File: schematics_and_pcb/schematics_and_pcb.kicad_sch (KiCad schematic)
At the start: 84 parts, among them J1 RND 205-00623, J2 RND 205-00627, J3 Motor con, J4 Conn_01x04_Male, J5 Conn_01x04_Male, Q1 PMV213SN, SW1 RND 210-00210, U1 MIC5235YM5-TR, U2 AP2125N-3.3TRG1, U3 PWM3389DM-T3QU, U4 STM32F411RETx, Y1 YLFXTAL029370

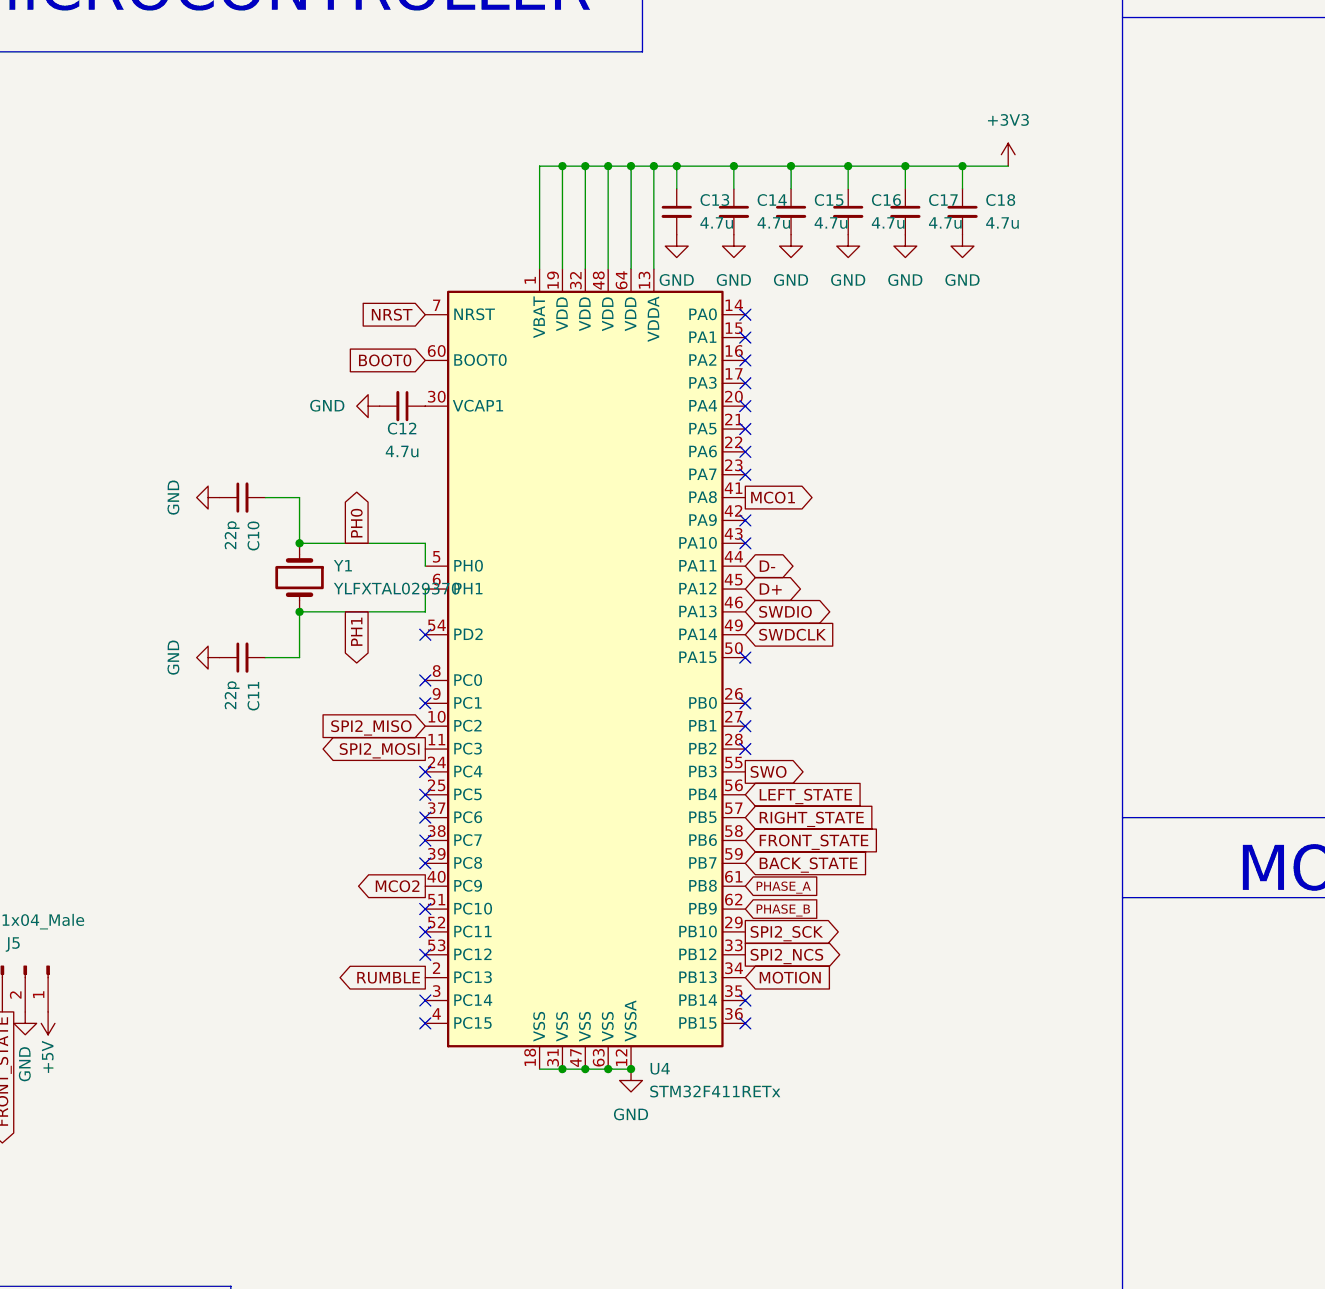
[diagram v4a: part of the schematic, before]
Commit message: added routes for all signals except buttons and scrollwheel
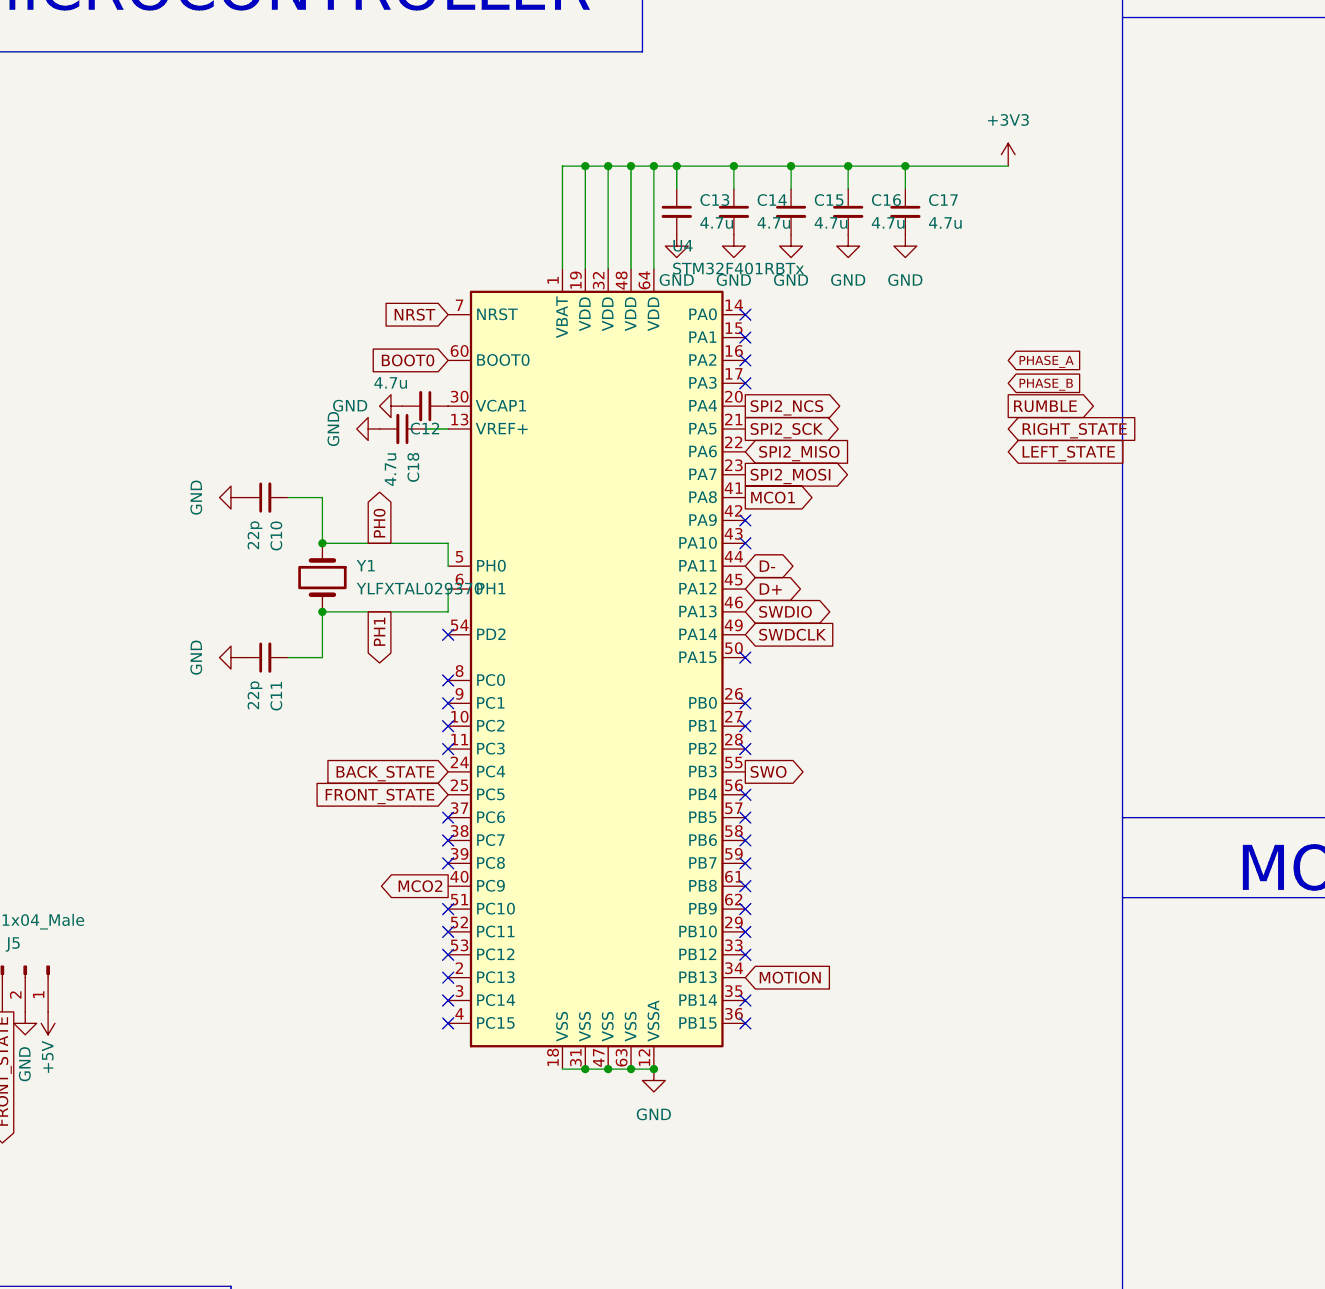
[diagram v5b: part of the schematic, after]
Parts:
- removed U4: STM32F411RETx, Package_QFP:LQFP-64_10x10mm_P0.5mm, symbol MCU_ST_STM32F4:STM32F411RETx
- added U4: STM32F401RBTx, Package_QFP:LQFP-64_10x10mm_P0.5mm, symbol MCU_ST_STM32F4:STM32F401RBTx
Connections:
- net +3V3: now also U4.1 (VBAT), U4.19 (VDD), U4.32 (VDD), U4.48 (VDD), U4.64 (VDD); no longer C18.1
- net BACK_STATE: now also U4.24 (PC4)
- net BOOT0: now also U4.60 (BOOT0)
- net D+: now also U4.45 (PA12)
- net D-: now also U4.44 (PA11)
- net FRONT_STATE: now also U4.25 (PC5)
- net GND: now also U4.12 (VSSA), U4.18 (VSS), U4.31 (VSS), U4.47 (VSS), U4.63 (VSS)
- net MCO1: now also U4.41 (PA8)
- net MCO2: now also U4.40 (PC9)
- net MOTION: now also U4.34 (PB13)
- net NRST: now also U4.7 (NRST)
- net PH0: now also U4.5 (PH0)
- net PH1: now also U4.6 (PH1)
- net SPI2_MISO: now also U4.22 (PA6)
- net SPI2_MOSI: now also U4.23 (PA7)
- net SPI2_NCS: now also U4.20 (PA4)
- net SPI2_SCK: now also U4.21 (PA5)
- net SWDCLK: now also U4.49 (PA14)
- net SWDIO: now also U4.46 (PA13)
- net SWO: now also U4.55 (PB3)
- net at C12.1: now also U4.30 (VCAP1)
- new net: C18.1, U4.13 (VREF+)
- no-connect marks 107 -> 112
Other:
- moved on the sheet: C10, C11, C12, Y1

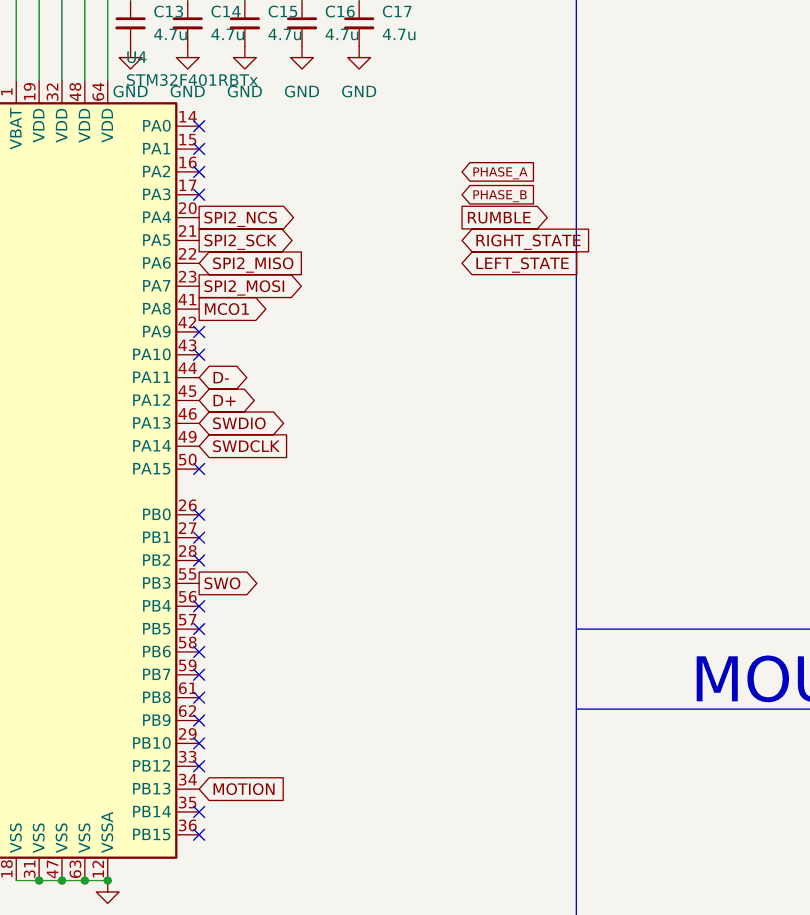
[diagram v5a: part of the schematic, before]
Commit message: added routes for all buttons
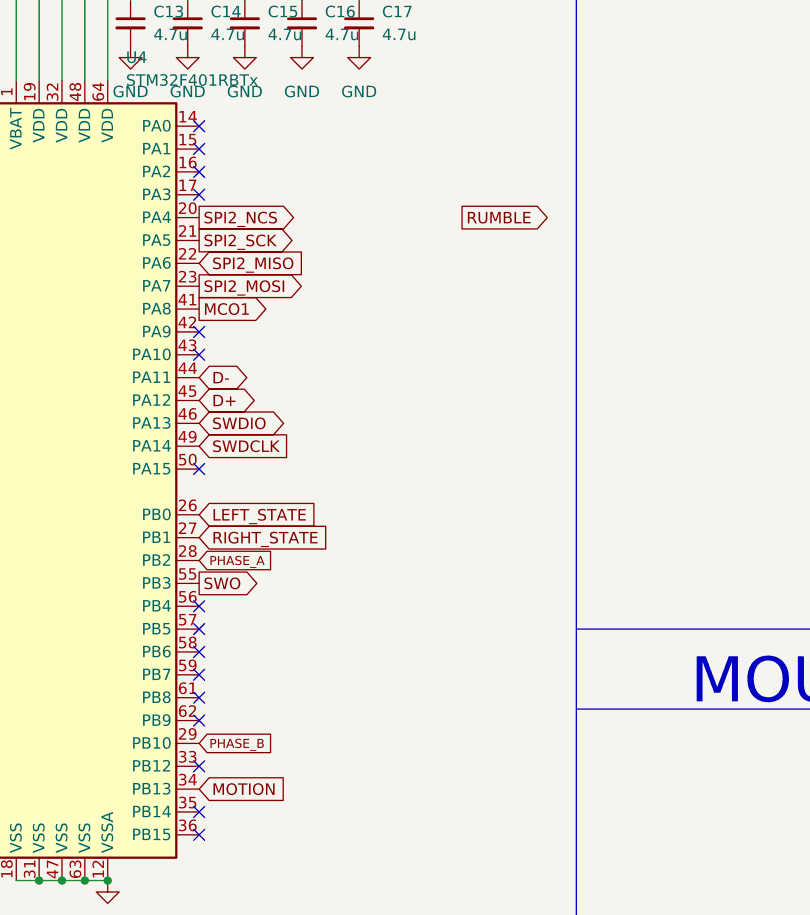
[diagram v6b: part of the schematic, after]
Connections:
- net LEFT_STATE: now also U4.26 (PB0)
- net PHASE_A: now also U4.28 (PB2)
- net PHASE_B: now also U4.29 (PB10)
- net RIGHT_STATE: now also U4.27 (PB1)
- no-connect marks 112 -> 108
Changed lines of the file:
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@@
   (no_connect (at 306.07 41.91))
   (no_connect (at 350.52 73.66))
-  (no_connect (at 233.68 100.33))
   (no_connect (at 325.12 90.17))
   (no_connect (at 233.68 59.69))
@@
   (no_connect (at 22.86 41.91))
   (no_connect (at 331.47 73.66))
-  (no_connect (at 233.68 105.41))
   (no_connect (at 374.65 59.69))
   (no_connect (at 374.65 44.45))
@@
   (no_connect (at 331.47 44.45))
   (no_connect (at 355.6 92.71))
-  (no_connect (at 233.68 125.73))
   (no_connect (at 355.6 59.69))
   (no_connect (at 144.78 189.23))
@@
   (no_connect (at 355.6 87.63))
   (no_connect (at 374.65 41.91))
-  (no_connect (at 233.68 102.87))
   (no_connect (at 325.12 92.71))
   (no_connect (at 200.66 100.33))
@@
     )
   )
-  (global_label "LEFT_STATE" (shape input) (at 262.89 72.39 0) (fields_autoplaced)
-    (effects (font (size 1.27 1.27)) (justify left))
-    (property "Intersheet References" "${INTERSHEET_REFS}" (id 0) (at 275.8864 72.3106 0)
-      (effects (font (size 1.27 1.27)) (justify left) hide)
-    )
-  )
-  (global_label "PHASE_A" (shape input) (at 262.89 62.23 0) (fields_autoplaced)
+  (global_label "LEFT_STATE" (shape input) (at 233.68 100.33 0) (fields_autoplaced)
+    (effects (font (size 1.27 1.27)) (justify left))
+    (property "Intersheet References" "${INTERSHEET_REFS}" (id 0) (at 246.6764 100.2506 0)
+      (effects (font (size 1.27 1.27)) (justify left) hide)
+    )
+  )
+  (global_label "PHASE_A" (shape input) (at 233.68 105.41 0) (fields_autoplaced)
     (effects (font (size 1 1)) (justify left))
-    (property "Intersheet References" "${INTERSHEET_REFS}" (id 0) (at 271.171 62.1675 0)
+    (property "Intersheet References" "${INTERSHEET_REFS}" (id 0) (at 241.961 105.3475 0)
       (effects (font (size 1 1)) (justify left) hide)
     )
@@
     )
   )
-  (global_label "RIGHT_STATE" (shape input) (at 262.89 69.85 0) (fields_autoplaced)
-    (effects (font (size 1.27 1.27)) (justify left))
-    (property "Intersheet References" "${INTERSHEET_REFS}" (id 0) (at 277.096 69.7706 0)
-      (effects (font (size 1.27 1.27)) (justify left) hide)
-    )
-  )
-  (global_label "PHASE_B" (shape input) (at 262.89 64.77 0) (fields_autoplaced)
+  (global_label "RIGHT_STATE" (shape input) (at 233.68 102.87 0) (fields_autoplaced)
+    (effects (font (size 1.27 1.27)) (justify left))
+    (property "Intersheet References" "${INTERSHEET_REFS}" (id 0) (at 247.886 102.7906 0)
+      (effects (font (size 1.27 1.27)) (justify left) hide)
+    )
+  )
+  (global_label "PHASE_B" (shape input) (at 233.68 125.73 0) (fields_autoplaced)
     (effects (font (size 1 1)) (justify left))
-    (property "Intersheet References" "${INTERSHEET_REFS}" (id 0) (at 271.3138 64.7075 0)
+    (property "Intersheet References" "${INTERSHEET_REFS}" (id 0) (at 242.1038 125.6675 0)
       (effects (font (size 1 1)) (justify left) hide)
     )

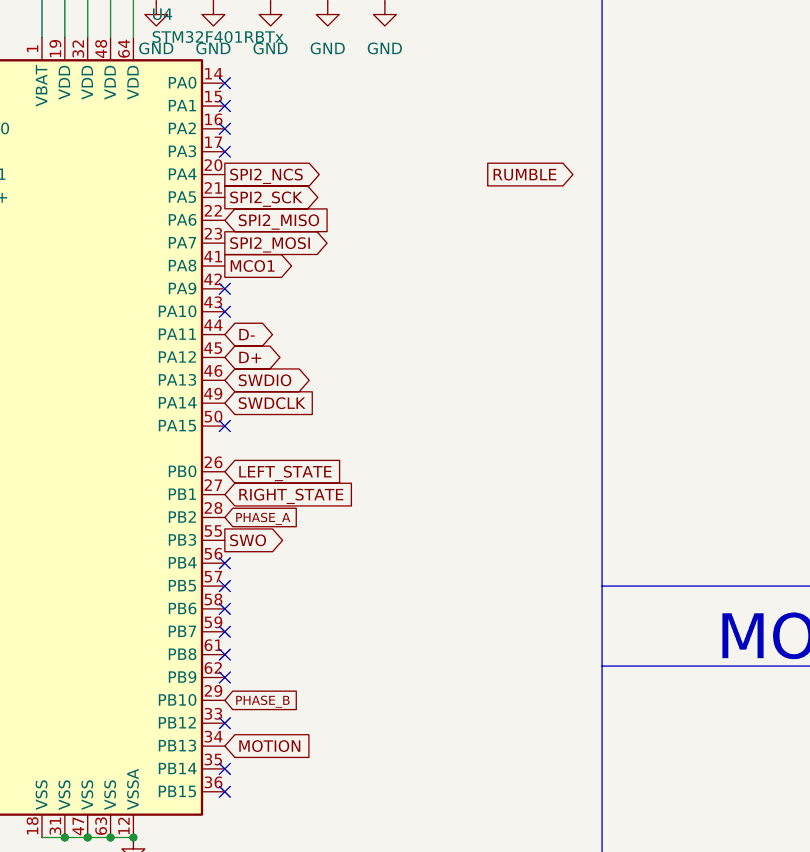
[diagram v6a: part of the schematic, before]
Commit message: added pin for the rumble
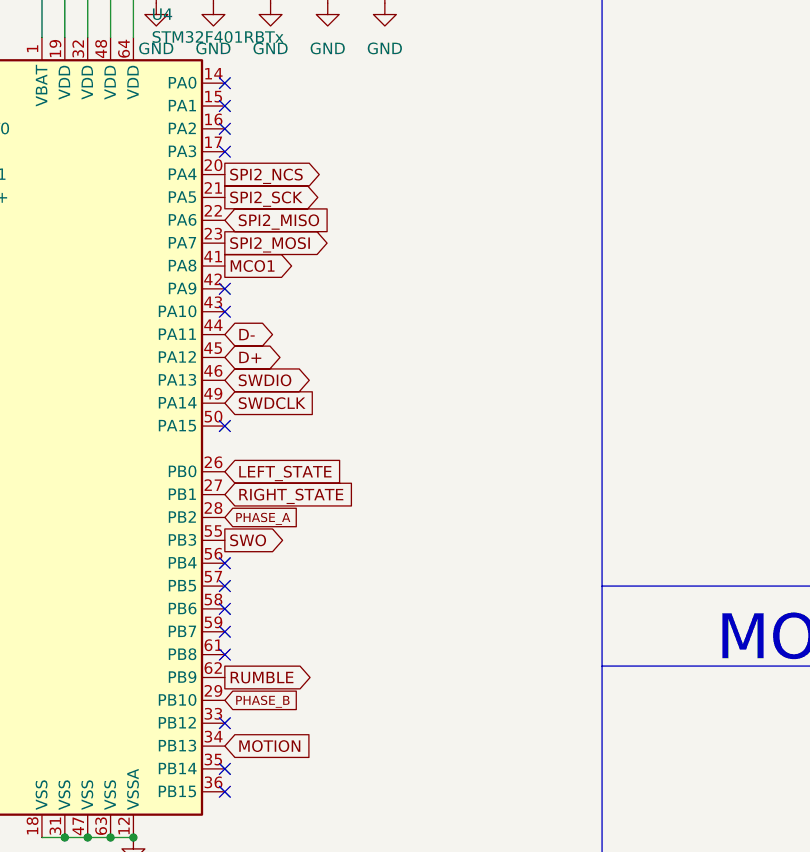
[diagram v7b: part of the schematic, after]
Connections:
- net RUMBLE: now also U4.62 (PB9)
- no-connect marks 108 -> 107
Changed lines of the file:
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@@
   (no_connect (at 331.47 78.74))
   (no_connect (at 303.53 166.37))
-  (no_connect (at 233.68 123.19))
   (no_connect (at 331.47 90.17))
   (no_connect (at 233.68 57.15))
@@
     )
   )
-  (global_label "RUMBLE" (shape output) (at 262.89 67.31 0) (fields_autoplaced)
-    (effects (font (size 1.27 1.27)) (justify left))
-    (property "Intersheet References" "${INTERSHEET_REFS}" (id 0) (at 272.8021 67.2306 0)
-      (effects (font (size 1.27 1.27)) (justify left) hide)
-    )
+  (global_label "RUMBLE" (shape output) (at 233.68 123.19 0) (fields_autoplaced)
+    (effects (font (size 1.27 1.27)) (justify left))
+    (property "Intersheet References" "${INTERSHEET_REFS}" (id 0) (at 243.5921 123.1106 0)
+      (effects (font (size 1.27 1.27)) (justify left) hide)
+    )

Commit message: some fixes
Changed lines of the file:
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@@
     (pin "3")
   )
-  (symbol (lib_id "Device:C_Small") (at 232.41 45.72 0) (unit 1)
+  (symbol (lib_id "Device:C_Small") (at 232.41 45.72 0) (mirror y) (unit 1)
     (in_bom yes) (on_board yes) (fields_autoplaced)
     (property "Reference" "C14" (id 0) (at 234.95 44.4562 0)
-      (effects (font (size 1.27 1.27)) (justify left))
+      (effects (font (size 1.27 1.27)) (justify right))
     )
     (property "Value" "4.7u" (id 1) (at 234.95 46.9962 0)
-      (effects (font (size 1.27 1.27)) (justify left))
+      (effects (font (size 1.27 1.27)) (justify right))
     )
     (property "Footprint" "Capacitor_SMD:C_0805_2012Metric_Pad1.18x1.45mm_HandSolder" (id 2) (at 232.41 45.72 0)
